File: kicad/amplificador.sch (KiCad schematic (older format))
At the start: 77 parts, among them J1 Screw_Terminal_01x01, J10 Conn_01x01_Male, J11 Conn_01x01_Male, J12 Conn_01x01_Male, J13 Conn_01x01_Male, J14 Conn_01x01_Male, J15 Conn_01x01_Male, J16 Screw_Terminal_01x01, J17 Screw_Terminal_01x01, J2 Conn_01x01_Male, J3 Conn_01x01_Male, J4 Conn_01x01_Male, J5 Conn_01x01_Male, J6 Conn_01x01_Male, J7 Screw_Terminal_01x01, J8 Screw_Terminal_01x01, J9 Conn_01x01_Male, Q1 MPSA92, Q10 MPSA42, Q11 BD135, Q12 BD136, Q13 BD135, Q14 BD136, Q15 2SD1047, Q16 2SD1047, Q17 2SB817, Q18 2SB817, Q2 MPSA42, Q3 MPSA92, Q4 MPSA42, Q5 MPSA92, Q6 MPSA92, Q7 MPSA42, Q8 MPSA92, Q9 MPSA42, U1 LM385D-1.2, U2 LM385D-1.2

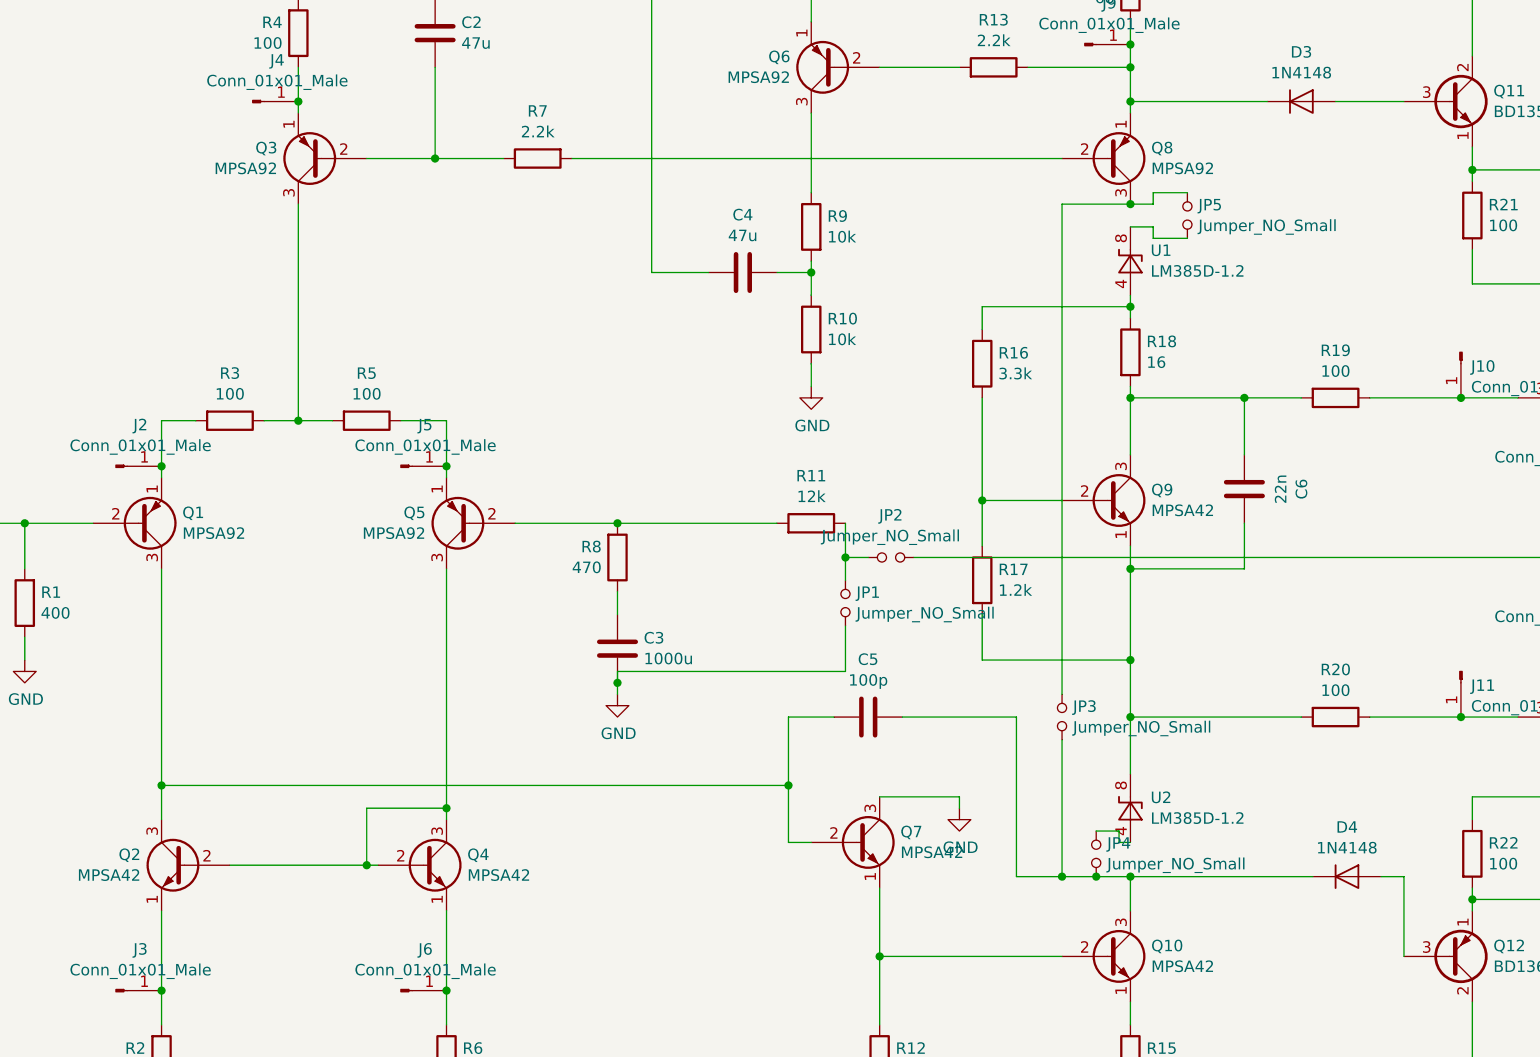
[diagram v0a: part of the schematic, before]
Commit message: cambios en los jumpers, ruteo avanzado
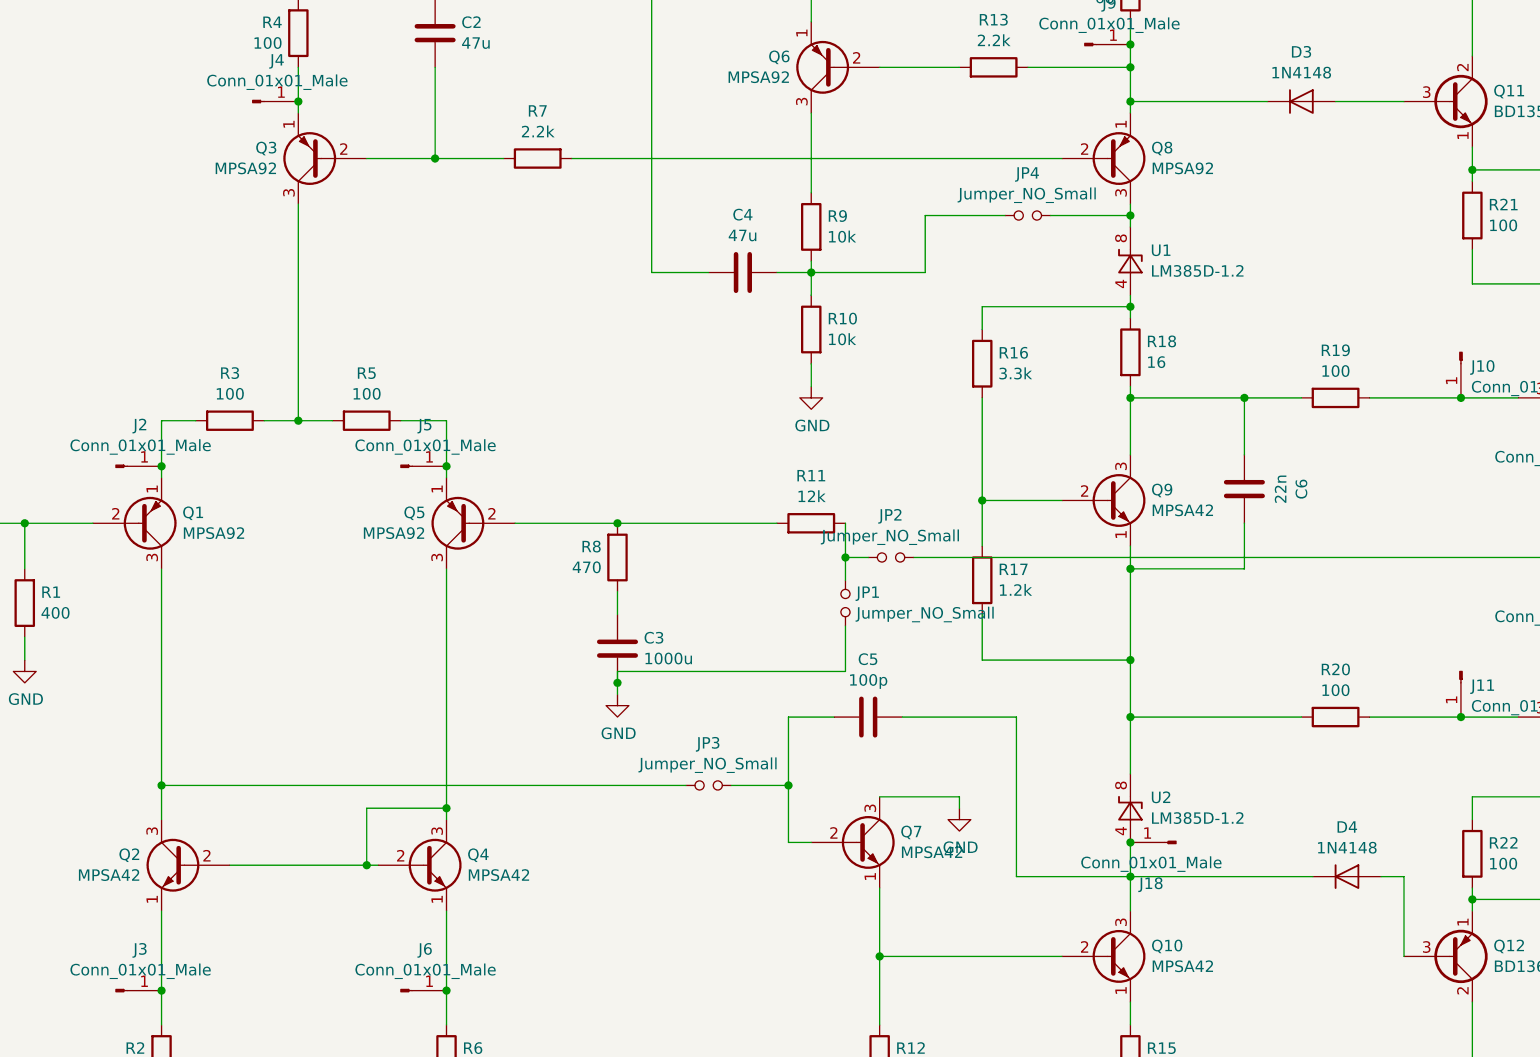
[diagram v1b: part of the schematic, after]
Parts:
- removed JP5: Jumper_NO_Small, kicad:SolderJumper-2_P1.3mm_Open_Pad1.0x1.5mm, symbol Device:Jumper_NO_Small
- added J18: Conn_01x01_Male, Connector_Pin:Pin_D0.7mm_L6.5mm_W1.8mm_FlatFork, symbol Connector:Conn_01x01_Male
- C1: footprint Capacitor_THT:C_Disc_D16.0mm_W5.0mm_P7.50mm -> Capacitor_THT:C_Disc_D10.0mm_W2.5mm_P5.00mm
- J1, J16, J17, J7, J8: footprint Connector_Wire:SolderWirePad_1x01_Drill2mm -> Connector_Wire:SolderWirePad_1x01_Drill0.8mm
- J10, J11, J12, J13, J14, J15, J2, J3, J4, J5, J6, J9: footprint Connector_Wire:SolderWirePad_1x01_Drill2mm -> Connector_Pin:Pin_D0.7mm_L6.5mm_W1.8mm_FlatFork
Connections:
- net at C4.1, R10.1, R9.2: now also JP4.1
- net at C5.1, D4.1 (K), Q10.3 (C): now also U2.4 (A), J18.1 (Pin_1); no longer JP3.2, JP4.2
- net at C5.2, Q7.2 (B): now also JP3.2; no longer Q1.3 (C), Q2.3 (C)
- net at JP3.1: now also Q1.3 (C), Q2.3 (C); no longer Q8.3 (C)
- net at U1.8 (K): now also JP4.2, Q8.3 (C)
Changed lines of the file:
@@
 F 0 "C1" V 948 3850 50  0000 C CNN
 F 1 "10u" V 1039 3850 50  0000 C CNN
-F 2 "Capacitor_THT:C_Disc_D16.0mm_W5.0mm_P7.50mm" H 1238 3700 50  0001 C CNN
+F 2 "Capacitor_THT:C_Disc_D10.0mm_W2.5mm_P5.00mm" H 1238 3700 50  0001 C CNN
 F 3 "~" H 1200 3850 50  0001 C CNN
 	1    1200 3850
@@
 	5350 5750 5350 6050
 Wire Wire Line
-	4950 4700 4950 5000
-Wire Wire Line
 	4950 5250 5050 5250
 Wire Wire Line
@@
 	5150 4700 4950 4700
 Wire Wire Line
-	2200 4050 2200 5000
-Wire Wire Line
-	2200 5000 4950 5000
-Connection ~ 2200 5000
-Wire Wire Line
-	2200 5000 2200 5150
-Connection ~ 4950 5000
-Wire Wire Line
-	4950 5000 4950 5250
-Wire Wire Line
 	5450 4700 5950 4700
 Wire Wire Line
 	5950 4700 5950 5400
-Wire Wire Line
-	5950 5400 6150 5400
 Wire Wire Line
 	7500 4700 7900 4700
@@
 F 0 "J8" V 5014 712 50  0000 R CNN
 F 1 "Screw_Terminal_01x01" V 4923 712 50  0000 R CNN
-F 2 "Connector_Wire:SolderWirePad_1x01_Drill2mm" H 5050 800 50  0001 C CNN
+F 2 "Connector_Wire:SolderWirePad_1x01_Drill0.8mm" H 5050 800 50  0001 C CNN
 F 3 "~" H 5050 800 50  0001 C CNN
 	1    5050 800
@@
 F 0 "J7" V 4472 7680 50  0000 L CNN
 F 1 "Screw_Terminal_01x01" V 4563 7680 50  0000 L CNN
-F 2 "Connector_Wire:SolderWirePad_1x01_Drill2mm" H 4600 7600 50  0001 C CNN
+F 2 "Connector_Wire:SolderWirePad_1x01_Drill0.8mm" H 4600 7600 50  0001 C CNN
 F 3 "~" H 4600 7600 50  0001 C CNN
 	1    4600 7600
@@
 F 0 "J1" H 768 3625 50  0000 C CNN
 F 1 "Screw_Terminal_01x01" H 768 3716 50  0000 C CNN
-F 2 "Connector_Wire:SolderWirePad_1x01_Drill2mm" H 850 3850 50  0001 C CNN
+F 2 "Connector_Wire:SolderWirePad_1x01_Drill0.8mm" H 850 3850 50  0001 C CNN
 F 3 "~" H 850 3850 50  0001 C CNN
 	1    850  3850
@@
 F 0 "J16" H 10130 4842 50  0000 L CNN
 F 1 "Screw_Terminal_01x01" H 10130 4751 50  0000 L CNN
-F 2 "Connector_Wire:SolderWirePad_1x01_Drill2mm" H 10050 4800 50  0001 C CNN
+F 2 "Connector_Wire:SolderWirePad_1x01_Drill0.8mm" H 10050 4800 50  0001 C CNN
 F 3 "~" H 10050 4800 50  0001 C CNN
 	1    10050 4800
@@
 F 0 "J17" H 10180 2792 50  0000 L CNN
 F 1 "Screw_Terminal_01x01" H 10180 2701 50  0000 L CNN
-F 2 "Connector_Wire:SolderWirePad_1x01_Drill2mm" H 10100 2750 50  0001 C CNN
+F 2 "Connector_Wire:SolderWirePad_1x01_Drill0.8mm" H 10100 2750 50  0001 C CNN
 F 3 "~" H 10100 2750 50  0001 C CNN
 	1    10100 2750
@@
 $EndComp
 $Comp
-L Device:Jumper_NO_Small JP5
-U 1 1 5D1DE1E4
-P 6700 2500
-F 0 "JP5" V 6654 2548 50  0000 L CNN
-F 1 "Jumper_NO_Small" V 6745 2548 50  0000 L CNN
-F 2 "kicad:SolderJumper-2_P1.3mm_Open_Pad1.0x1.5mm" H 6700 2500 50  0001 C CNN
-F 3 "~" H 6700 2500 50  0001 C CNN
-	1    6700 2500
-	0    1    1    0
-$EndComp
-Wire Wire Line
-	6550 2400 6550 2450
-Wire Wire Line
-	6550 2450 6450 2450
-Wire Wire Line
-	6550 2400 6700 2400
-Wire Wire Line
-	6450 2550 6550 2550
-Wire Wire Line
-	6550 2550 6550 2600
-Wire Wire Line
-	6550 2600 6700 2600
-$Comp
-L Device:Jumper_NO_Small JP4
-U 1 1 5D1EAB70
-P 6300 5300
-F 0 "JP4" V 6254 5348 50  0000 L CNN
-F 1 "Jumper_NO_Small" V 6345 5348 50  0000 L CNN
-F 2 "kicad:SolderJumper-2_P1.3mm_Open_Pad1.0x1.5mm" H 6300 5300 50  0001 C CNN
-F 3 "~" H 6300 5300 50  0001 C CNN
-	1    6300 5300
-	0    1    1    0
-$EndComp
-Connection ~ 6300 5400
-Wire Wire Line
-	6300 5400 6450 5400
-Wire Wire Line
-	6300 5200 6400 5200
-Wire Wire Line
-	6400 5200 6400 5250
-Wire Wire Line
-	6400 5250 6450 5250
-$Comp
-L Device:Jumper_NO_Small JP3
-U 1 1 5D1F173A
-P 6150 4700
-F 0 "JP3" V 6104 4748 50  0000 L CNN
-F 1 "Jumper_NO_Small" V 6195 4748 50  0000 L CNN
-F 2 "kicad:SolderJumper-2_P1.3mm_Open_Pad1.0x1.5mm" H 6150 4700 50  0001 C CNN
-F 3 "~" H 6150 4700 50  0001 C CNN
-	1    6150 4700
-	0    1    1    0
-$EndComp
-Wire Wire Line
-	6150 4800 6150 5400
-Connection ~ 6150 5400
-Wire Wire Line
-	6150 5400 6300 5400
-Wire Wire Line
-	6150 2450 6450 2450
-Connection ~ 6450 2450
-Wire Wire Line
-	6150 2450 6150 4600
-$Comp
 L Connector:Conn_01x01_Male J3
 U 1 1 5D1FF032
@@
 F 0 "J3" H 2108 6081 50  0000 C CNN
 F 1 "Conn_01x01_Male" H 2108 5990 50  0000 C CNN
-F 2 "Connector_Wire:SolderWirePad_1x01_Drill2mm" H 2000 5900 50  0001 C CNN
+F 2 "Connector_Pin:Pin_D0.7mm_L6.5mm_W1.8mm_FlatFork" H 2000 5900 50  0001 C CNN
 F 3 "~" H 2000 5900 50  0001 C CNN
 	1    2000 5900
@@
 F 0 "J6" H 3358 6081 50  0000 C CNN
 F 1 "Conn_01x01_Male" H 3358 5990 50  0000 C CNN
-F 2 "Connector_Wire:SolderWirePad_1x01_Drill2mm" H 3250 5900 50  0001 C CNN
+F 2 "Connector_Pin:Pin_D0.7mm_L6.5mm_W1.8mm_FlatFork" H 3250 5900 50  0001 C CNN
 F 3 "~" H 3250 5900 50  0001 C CNN
 	1    3250 5900
@@
 F 0 "J4" H 2708 2181 50  0000 C CNN
 F 1 "Conn_01x01_Male" H 2708 2090 50  0000 C CNN
-F 2 "Connector_Wire:SolderWirePad_1x01_Drill2mm" H 2600 2000 50  0001 C CNN
+F 2 "Connector_Pin:Pin_D0.7mm_L6.5mm_W1.8mm_FlatFork" H 2600 2000 50  0001 C CNN
 F 3 "~" H 2600 2000 50  0001 C CNN
 	1    2600 2000
@@
 F 0 "J2" H 2108 3781 50  0000 C CNN
 F 1 "Conn_01x01_Male" H 2108 3690 50  0000 C CNN
-F 2 "Connector_Wire:SolderWirePad_1x01_Drill2mm" H 2000 3600 50  0001 C CNN
+F 2 "Connector_Pin:Pin_D0.7mm_L6.5mm_W1.8mm_FlatFork" H 2000 3600 50  0001 C CNN
 F 3 "~" H 2000 3600 50  0001 C CNN
 	1    2000 3600
@@
 F 0 "J5" H 3358 3781 50  0000 C CNN
 F 1 "Conn_01x01_Male" H 3358 3690 50  0000 C CNN
-F 2 "Connector_Wire:SolderWirePad_1x01_Drill2mm" H 3250 3600 50  0001 C CNN
+F 2 "Connector_Pin:Pin_D0.7mm_L6.5mm_W1.8mm_FlatFork" H 3250 3600 50  0001 C CNN
 F 3 "~" H 3250 3600 50  0001 C CNN
 	1    3250 3600
@@
 F 0 "J9" H 6358 1931 50  0000 C CNN
 F 1 "Conn_01x01_Male" H 6358 1840 50  0000 C CNN
-F 2 "Connector_Wire:SolderWirePad_1x01_Drill2mm" H 6250 1750 50  0001 C CNN
+F 2 "Connector_Pin:Pin_D0.7mm_L6.5mm_W1.8mm_FlatFork" H 6250 1750 50  0001 C CNN
 F 3 "~" H 6250 1750 50  0001 C CNN
 	1    6250 1750
@@
 F 0 "J14" H 9158 3881 50  0000 C CNN
 F 1 "Conn_01x01_Male" H 9158 3790 50  0000 C CNN
-F 2 "Connector_Wire:SolderWirePad_1x01_Drill2mm" H 9050 3700 50  0001 C CNN
+F 2 "Connector_Pin:Pin_D0.7mm_L6.5mm_W1.8mm_FlatFork" H 9050 3700 50  0001 C CNN
 F 3 "~" H 9050 3700 50  0001 C CNN
 	1    9050 3700
@@
 F 0 "J15" H 9158 4531 50  0000 C CNN
 F 1 "Conn_01x01_Male" H 9158 4440 50  0000 C CNN
-F 2 "Connector_Wire:SolderWirePad_1x01_Drill2mm" H 9050 4350 50  0001 C CNN
+F 2 "Connector_Pin:Pin_D0.7mm_L6.5mm_W1.8mm_FlatFork" H 9050 4350 50  0001 C CNN
 F 3 "~" H 9050 4350 50  0001 C CNN
 	1    9050 4350
@@
 F 0 "J10" V 7962 3144 50  0000 L CNN
 F 1 "Conn_01x01_Male" V 8053 3144 50  0000 L CNN
-F 2 "Connector_Wire:SolderWirePad_1x01_Drill2mm" H 7900 3100 50  0001 C CNN
+F 2 "Connector_Pin:Pin_D0.7mm_L6.5mm_W1.8mm_FlatFork" H 7900 3100 50  0001 C CNN
 F 3 "~" H 7900 3100 50  0001 C CNN
 	1    7900 3100
@@
 F 0 "J11" V 7962 4544 50  0000 L CNN
 F 1 "Conn_01x01_Male" V 8053 4544 50  0000 L CNN
-F 2 "Connector_Wire:SolderWirePad_1x01_Drill2mm" H 7900 4500 50  0001 C CNN
+F 2 "Connector_Pin:Pin_D0.7mm_L6.5mm_W1.8mm_FlatFork" H 7900 4500 50  0001 C CNN
 F 3 "~" H 7900 4500 50  0001 C CNN
 	1    7900 4500
@@
 F 0 "J13" H 8358 4531 50  0000 C CNN
 F 1 "Conn_01x01_Male" H 8358 4440 50  0000 C CNN
-F 2 "Connector_Wire:SolderWirePad_1x01_Drill2mm" H 8250 4350 50  0001 C CNN
+F 2 "Connector_Pin:Pin_D0.7mm_L6.5mm_W1.8mm_FlatFork" H 8250 4350 50  0001 C CNN
 F 3 "~" H 8250 4350 50  0001 C CNN
 	1    8250 4350
@@
 F 0 "J12" H 8358 3831 50  0000 C CNN
 F 1 "Conn_01x01_Male" H 8358 3740 50  0000 C CNN
-F 2 "Connector_Wire:SolderWirePad_1x01_Drill2mm" H 8250 3650 50  0001 C CNN
+F 2 "Connector_Pin:Pin_D0.7mm_L6.5mm_W1.8mm_FlatFork" H 8250 3650 50  0001 C CNN
 F 3 "~" H 8250 3650 50  0001 C CNN
 	1    8250 3650
@@
 	9250 4350 9250 4300
 Connection ~ 9250 4350
+Wire Wire Line
+	5950 5400 6450 5400
+Wire Wire Line
+	6450 5250 6450 5400
+$Comp
+L Connector:Conn_01x01_Male J18
+U 1 1 5D27FE44
+P 6650 5250
+F 0 "J18" H 6758 5431 50  0000 C CNN
+F 1 "Conn_01x01_Male" H 6758 5340 50  0000 C CNN
+F 2 "Connector_Pin:Pin_D0.7mm_L6.5mm_W1.8mm_FlatFork" H 6650 5250 50  0001 C CNN
+F 3 "~" H 6650 5250 50  0001 C CNN
+	1    6650 5250
+	-1   0    0    1
+$EndComp
+Connection ~ 6450 5250
+$Comp
+L Device:Jumper_NO_Small JP3
+U 1 1 5D280930
+P 4600 5000
+F 0 "JP3" H 4600 5185 50  0000 C CNN
+F 1 "Jumper_NO_Small" H 4600 5094 50  0000 C CNN
+F 2 "kicad:SolderJumper-2_P1.3mm_Open_Pad1.0x1.5mm" H 4600 5000 50  0001 C CNN
+F 3 "~" H 4600 5000 50  0001 C CNN
+	1    4600 5000
+	1    0    0    -1
+$EndComp
+Wire Wire Line
+	4700 5000 4950 5000
+Wire Wire Line
+	4950 4700 4950 5000
+Connection ~ 4950 5000
+Wire Wire Line
+	4950 5000 4950 5250
+Wire Wire Line
+	4500 5000 2200 5000
+Wire Wire Line
+	2200 4050 2200 5000
+Connection ~ 2200 5000
+Wire Wire Line
+	2200 5000 2200 5150
+$Comp
+L Device:Jumper_NO_Small JP4
+U 1 1 5D28F36B
+P 6000 2500
+F 0 "JP4" H 6000 2685 50  0000 C CNN
+F 1 "Jumper_NO_Small" H 6000 2594 50  0000 C CNN
+F 2 "kicad:SolderJumper-2_P1.3mm_Open_Pad1.0x1.5mm" H 6000 2500 50  0001 C CNN
+F 3 "~" H 6000 2500 50  0001 C CNN
+	1    6000 2500
+	1    0    0    -1
+$EndComp
+Wire Wire Line
+	6100 2500 6450 2500
+Wire Wire Line
+	6450 2450 6450 2500
+Connection ~ 6450 2500
+Wire Wire Line
+	6450 2500 6450 2550
+Wire Wire Line
+	5900 2500 5550 2500
+Wire Wire Line
+	5550 2500 5550 2750
+Wire Wire Line
+	5550 2750 5050 2750
 $EndSCHEMATC
